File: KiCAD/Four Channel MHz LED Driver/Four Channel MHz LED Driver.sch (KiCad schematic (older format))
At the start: 39 parts

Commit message: First draft of Teensy pin allocation
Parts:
- added J?: Conn_01x05_Male, Custom Footprints:Ref_only, symbol Custom_parts:Conn_01x05_Male
- added J?: Conn_01x04_Male, Custom Footprints:Ref_only, symbol Custom_parts:Conn_01x04_Male
- added U?: Teensy3.6, symbol Custom_parts:Teensy3.6
- U?: value S18V20F12_12V_DC -> S34V32F12_12V_DC; footprint (none) -> Custom Footprints:S18V20F12_12V_DC
- U?: value ADP7118AUJZ-5.0-R7 -> ADP7134AUJZ-5.0-R7
- U? (x4): value TMUX1204DGSR -> TMUX1324DGSR
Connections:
- net 12V: now also J?.~ (Pin_4)
- net 3.3V: now also U?.15 (3.3V), U?.51 (3.3V)
- net 5V: now also U?.53 (VIN)
- net GND: now also RN?.2 (R2.1), RN?.4 (R4.1), RN?.6 (R6.1), RN?.8 (R8.1), J?.~ (Pin_4), J?.~ (Pin_5), U?.1 (GND), U?.39 (GND), U?.52 (AGND); no longer C?.1, RN?.11 (R6.2), RN?.13 (R4.2), RN?.15 (R2.2), RN?.9 (R8.2), U?.8 (GND), U?.9 (GND)
- net Isense_1: now also J?.1 (IN1), RN?.1 (R1.1); no longer RN?.16 (R1.2)
- net Isense_2: now also J?.2 (IN2), RN?.3 (R3.1); no longer RN?.14 (R3.2)
- net Isense_3: now also J?.1 (IN1), RN?.5 (R5.1); no longer RN?.12 (R5.2)
- net Isense_4: now also J?.2 (IN2), RN?.7 (R7.1); no longer RN?.10 (R7.2)
- net Vin: now also J?.~ (Pin_5)
- net SCK0: now reaches U?.10 (SCLK)
- net SCK0: now also U?.5 (SCK), U?.19 (27_RX1)
- net MOSI0: now reaches U?.8 (DIN)
- net MOSI0: now also U?.6 (SDI), U?.20 (28)
- net 25: now reaches U?.9 (~SYNC)
- net 25: now also U?.17 (25)
- net 24: now reaches U?.4 (*CS)
- net 24: now also U?.16 (24)
- net OA1_input: now reaches U?.8 (D)
- net OA2_input: now reaches U?.8 (D)
- net OA3_input: now reaches U?.8 (D)
- net OA4_input: now reaches U?.8 (D)
- net A-D_IO_1 renamed 35
- net 35: now also U?.32 (35_A16_PWM)
- net A-D_IO_2 renamed 34
- net 34: now also U?.31 (34_A15_RX5_CAN1TX_SDA0)
- net A-D_IO_3 renamed 33
- net 33: now also U?.30 (33_A14_TX5_CAN1TX_SCL0)
- net A-D_IO_4 renamed 32
- net 32: now also U?.24 (32_A13_TX4_SCK1)
- net analog_select_1 renamed 3
- net 3: now also U?.5 (3_PWM_CAN0TX_SCL2)
- net analog_select_2 renamed 5
- net 5: now also U?.7 (5_PWM_TX1_MISO1)
- net analog_select_3 renamed 7
- net 7: now also U?.9 (7_RX3_MISO0_SCL0)
- net analog_select_4 renamed 9
- net 9: now also U?.11 (9_PWM_RX2_CS0)
- net interline_1 renamed 2
- net 2: now also U?.4 (2_PWM)
- net interline_2 renamed 4
- net 4: now also U?.6 (4_PWM_CAN0RX_SDA2)
- net interline_3 renamed 6
- net 6: now also U?.8 (6_PWM)
- net interline_4 renamed 8
- net 8: now also U?.10 (8_TX3_MISO0_SDA0)
- new net: C?.1, U?.8 (GND), U?.9 (GND)
- new net A0_ADC0: RN?.13 (R4.2), RN?.14 (R3.2), U?.41 (14_A0_PWM_SCK0)
- new net A1_ADC0: RN?.15 (R2.2), RN?.16 (R1.2), U?.42 (15_A1_CS0_TOUCH)
- new net A33_DAC1: RN?.10 (R7.2), RN?.9 (R8.2), U?.37 (A21_DAC0)
- new net A34_DAC1: RN?.11 (R6.2), RN?.12 (R5.2), U?.38 (A22_DAC1)
- no-connect marks 3 -> 44
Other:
- note added: "----ADC0-----"
- note added: "----ADC1-----"
- note added: "A/D IO 1"
- note added: "A/D IO 2"
- note added: "A/D IO 3"
- note added: "A/D IO 4"
- note added: "Analog select 1\n"
- note added: "Analog select 2\n"
- note added: "Analog select 3\n"
- note added: "Analog select 4\n"
- note added: "Current sense voltage ouput"
- note added: "DAC CS"
- note added: "Digipot CS"
- note added: "Ext fan PWM"
- note added: "Ext temp"
- note added: "Header pins\nto connect\n12V SEPIC \nDC-DC \nconverter"
- note added: "Interline PWM 1"
- note added: "Interline PWM 2"
- note added: "Interline PWM 3"
- note added: "Interline PWM 4"
- note added: "Internal 4-channel ADC AWG with digipot current limit"
- note added: "Internal fan PWM"
- note added: "Isense_1"
- note added: "Isense_2"
- note added: "Isense_3"
- note added: "Isense_4"
- note added: "LED pot 1"
- note added: "LED pot 2"
- note added: "LED pot 3"
- note added: "LED pot 4"
- note added: "MOSFET temp 1"
- note added: "MOSFET temp 2"
- note added: "MOSFET temp 3"
- note added: "MOSFET temp 4"
- note added: "Manual/Auto Switch"
- note added: "Op-amp input mux"
- note added: "Pool external analog inputs"
- note added: "Resistor temp 1"
- note added: "Resistor temp 2"
- note added: "Resistor temp 3"
- note added: "Resistor temp 4"
- note added: "Status LED 1"
- note added: "Status LED 2"
- note added: "Status LED 3"
- note added: "Status LED 4"
- note added: "over-temp alarm"
- note removed: "Internal 4-channel AWG with current limit"
- moved on the sheet: C?, D?, J?, RN?, SW?, U?

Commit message: Reduce input impedance to 4.7k
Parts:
- removed RN?: 10k, Custom Footprints:Bourns_16-SOIC_8x_r-pack, symbol Device:R_Pack08
- added RN?: 4.7k, Custom Footprints:Bourns_16-SOIC_8x_r-pack, symbol Device:R_Pack08
- RN?: value 10k -> 4.7k; Part # 4816P-T01-103LF -> 4816P-T01-472LF
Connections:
- net GND: now also RN?.2 (R2.1), RN?.4 (R4.1), RN?.6 (R6.1), RN?.8 (R8.1)
- net Isense_1: now also RN?.1 (R1.1)
- net Isense_2: now also RN?.3 (R3.1)
- net Isense_3: now also RN?.5 (R5.1)
- net Isense_4: now also RN?.7 (R7.1)
- net A0_ADC0 renamed A0
- net A0: now also RN?.13 (R4.2), RN?.14 (R3.2)
- net A1_ADC0 renamed A1
- net A1: now also RN?.15 (R2.2), RN?.16 (R1.2)
- net A33_DAC1 renamed A33
- net A33: now also RN?.10 (R7.2), RN?.9 (R8.2)
- net A34_DAC1 renamed A34
- net A34: now also RN?.11 (R6.2), RN?.12 (R5.2)
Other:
- note added: "I/O maximum voltage: 27V"
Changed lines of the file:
@@
 P 2200 8150
 F 0 "RN?" V 1583 8150 50  0000 C CNN
-F 1 "10k" V 1674 8150 50  0000 C CNN
+F 1 "4.7k" V 1674 8150 50  0000 C CNN
 F 2 "Custom Footprints:Bourns_16-SOIC_8x_r-pack" V 2675 8150 50  0001 C CNN
 F 3 "file://media.digikey.com/api/videos/videoplayer/smallplayer/N0706.pdf" H 2200 8150 50  0001 C CNN
 F 4 "Bourns Inc." V 2200 8150 50  0001 C CNN "Manufacturer"
-F 5 "4816P-T01-103LF" V 2200 8150 50  0001 C CNN "Part #"
+F 5 "4816P-T01-472LF" V 2200 8150 50  0001 C CNN "Part #"
 	1    2200 8150
 	0    1    1    0
@@
 	1    1400 1600
 	0    -1   -1   0
-$EndComp
-$Comp
-L Device:R_Pack08 RN?
-U 1 1 5F51AB0E
-P 5350 9400
-F 0 "RN?" V 4733 9400 50  0000 C CNN
-F 1 "10k" V 4824 9400 50  0000 C CNN
-F 2 "Custom Footprints:Bourns_16-SOIC_8x_r-pack" V 5825 9400 50  0001 C CNN
-F 3 "file://media.digikey.com/api/videos/videoplayer/smallplayer/N0706.pdf" H 5350 9400 50  0001 C CNN
-F 4 "Bourns Inc." V 5350 9400 50  0001 C CNN "Manufacturer"
-F 5 "4816P-T01-103LF" V 5350 9400 50  0001 C CNN "Part #"
-	1    5350 9400
-	0    1    1    0
 $EndComp
 Text Label 5150 9000 2    50   ~ 0
@@
 Op-amp input mux
 Text Label 21950 2250 0    50   ~ 0
-A0_ADC0
+A0
 Text Label 21950 2550 0    50   ~ 0
-A34_DAC1
+A34
 Text Label 21950 2650 0    50   ~ 0
-A33_DAC1
+A33
 Text Label 19650 2850 2    50   ~ 0
 SCK0
@@
 MOSI0
 Text Label 5550 9050 0    50   ~ 0
-A1_ADC0
+A1
 Text Label 21950 2150 0    50   ~ 0
-A1_ADC0
+A1
 Text Label 5550 9250 0    50   ~ 0
-A0_ADC0
+A0
 Text Label 5550 9450 0    50   ~ 0
-A34_DAC1
+A34
 Text Label 5550 9650 0    50   ~ 0
-A33_DAC1
+A33
 Text Label 3950 5750 2    50   ~ 0
 SCK0
@@
 Text Notes 23100 3300 1    50   ~ 0
 ----ADC1-----
-Text Notes 18950 2350 0    50   ~ 0
+Text Notes 18650 2350 0    50   ~ 0
 Status LED 4
-Text Notes 18950 2250 0    50   ~ 0
+Text Notes 18650 2250 0    50   ~ 0
 Status LED 3
 Text Label 19650 2050 2    50   ~ 0
@@
 Text Label 19650 1750 2    50   ~ 0
 6
-Text Notes 18950 1250 0    50   ~ 0
+Text Notes 18600 1250 0    50   ~ 0
 Status LED 2
-Text Notes 18950 1150 0    50   ~ 0
+Text Notes 18600 1150 0    50   ~ 0
 Status LED 1
 Text Notes 19550 1950 2    50   ~ 0
@@
 Text Notes 18950 2050 0    50   ~ 0
 Analog select 4\n
+$Comp
+L Device:R_Pack08 RN?
+U 1 1 5F57894B
+P 5350 9400
+F 0 "RN?" V 4733 9400 50  0000 C CNN
+F 1 "4.7k" V 4824 9400 50  0000 C CNN
+F 2 "Custom Footprints:Bourns_16-SOIC_8x_r-pack" V 5825 9400 50  0001 C CNN
+F 3 "file://media.digikey.com/api/videos/videoplayer/smallplayer/N0706.pdf" H 5350 9400 50  0001 C CNN
+F 4 "Bourns Inc." V 5350 9400 50  0001 C CNN "Manufacturer"
+F 5 "4816P-T01-472LF" V 5350 9400 50  0001 C CNN "Part #"
+	1    5350 9400
+	0    1    1    0
+$EndComp
+Text Notes 900  8700 1    59   ~ 0
+I/O maximum voltage: 27V
 $EndSCHEMATC

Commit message: Update license
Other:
- note added: "Distribute external analog inputs"
- note removed: "Pool external analog inputs"
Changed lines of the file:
@@
 Text Notes 2900 8450 2    50   ~ 0
 A/D IO 4
-Text Notes 3800 7650 0    59   ~ 0
-Pool external analog inputs
+Text Notes 3600 7650 0    59   ~ 0
+Distribute external analog inputs
 Text Notes 22250 1450 0    50   ~ 0
 LED pot 2

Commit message: Split analog inputs between ADC0 and ADC1
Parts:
- U?: value MCP4351-502E_ST -> MCP4211-502E_ST
- U?: value S34V32F12_12V_DC -> S20V18F12_12V_DC
- U?: value ADP7134AUJZ-5.0-R7 -> ADP7120AUJZ-5.0-R7
- U? (x4): value TMUX1324DGSR -> TMUX1184DGSR
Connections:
- removed net 32: D?.3, RN?.9 (R8.2), U?.24 (32_A13_TX4_SCK1)
- removed net 33: D?.6, RN?.10 (R7.2), U?.30 (33_A14_TX5_CAN1TX_SCL0)
- removed net 34: D?.3, RN?.11 (R6.2), U?.31 (34_A15_RX5_CAN1TX_SDA0)
- removed net 35: D?.6, RN?.12 (R5.2), U?.32 (35_A16_PWM)
- net A0: no longer names the net of RN?.13 (R4.2), RN?.14 (R3.2)
- net A0: no longer U?.41 (14_A0_PWM_SCK0)
- net A1: no longer names the net of RN?.15 (R2.2), RN?.16 (R1.2)
- net A1: no longer U?.42 (15_A1_CS0_TOUCH)
- net A33: no longer names the net of RN?.10 (R7.2), RN?.9 (R8.2)
- net A33: no longer U?.37 (A21_DAC0)
- net A34: no longer names the net of RN?.11 (R6.2), RN?.12 (R5.2)
- net A34: no longer U?.38 (A22_DAC1)
- new net 18: RN?.9 (R8.2)
- new net 19: RN?.10 (R7.2)
- new net 20: RN?.11 (R6.2)
- new net 21: RN?.12 (R5.2)
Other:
- note added: "-------ADC0------"
- note added: "--ADC1--"
- note added: "ADC0"
- note added: "ADC1"
- note added: "I/O maximum voltage: 27V (160mW)\nNiDaq PCI-6110 is +/- 10V 5mA\nTherefore, minimum impedance is 2000 Ohms"
- note added: "https://forum.pjrc.com/attachment.php?attachmentid=10666&d=1495536536"
- note removed: "----ADC0-----"
- note removed: "----ADC1-----"
- note removed: "I/O maximum voltage: 27V"
- moved on the sheet: D?, U?

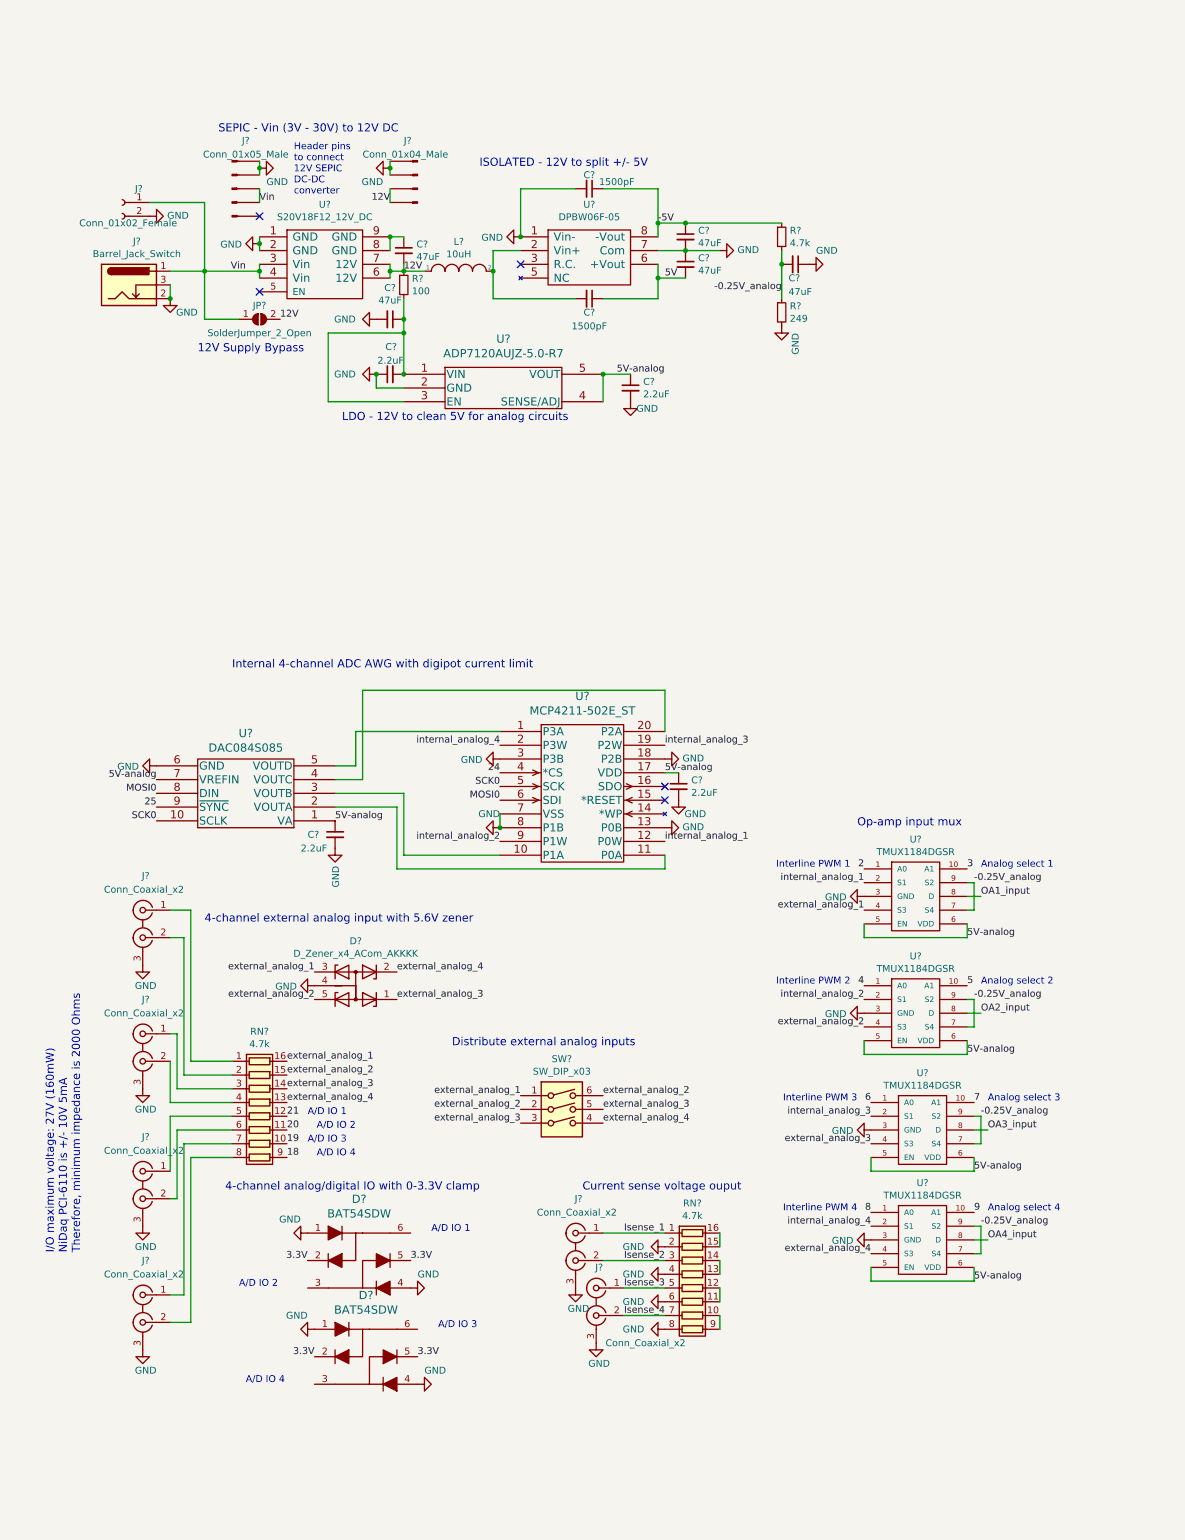
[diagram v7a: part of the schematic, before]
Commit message: Add LED connectors switch to RJ45 for IO
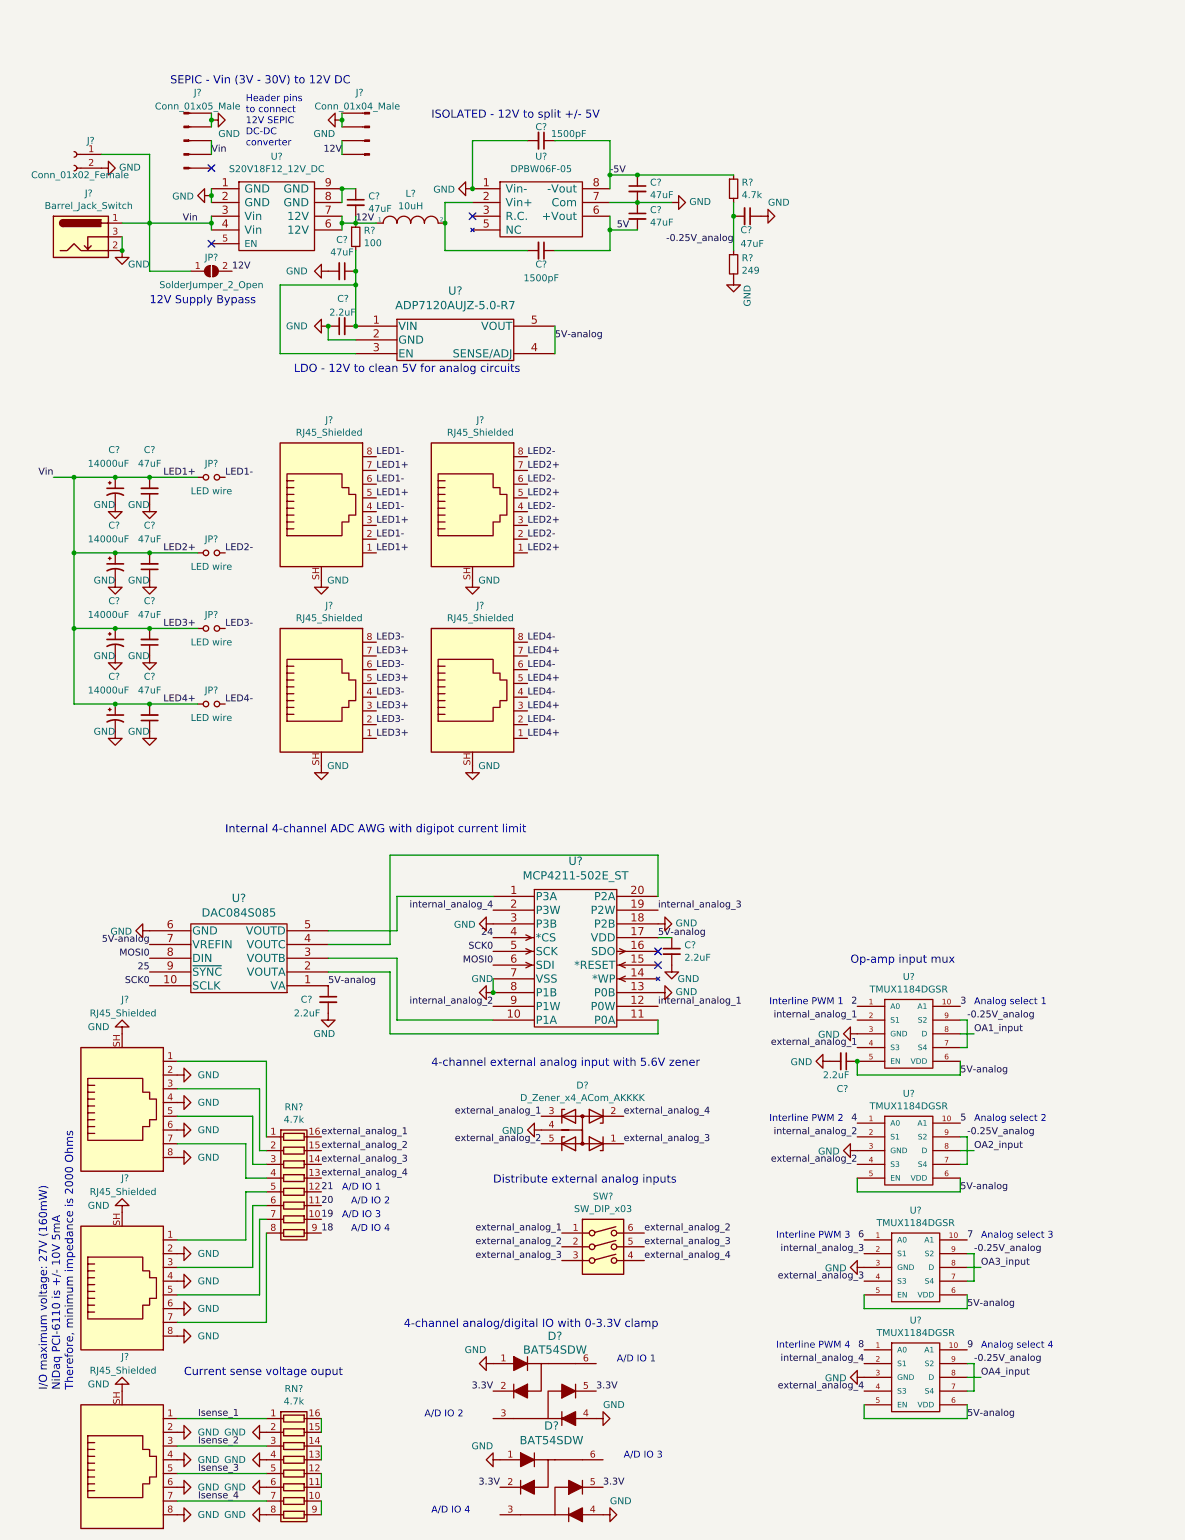
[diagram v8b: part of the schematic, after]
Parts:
- removed C?: 2.2uF, Custom Footprints:0508_Capacitor, symbol Device:C_Small
- removed J? (x6): Conn_Coaxial_x2, Custom Footprints:031-6575_2x_BNC, symbol Connector:Conn_Coaxial_x2
- added C? (x4): 14000uF, Capacitor_THT:CP_Radial_D18.0mm_P7.50mm, symbol Device:CP1_Small
- added C? (x4): 47uF, Capacitor_SMD:C_1206_3216Metric, symbol Device:C_Small
- added C?: 2.2uF, Custom Footprints:0508_Capacitor, symbol Device:C_Small
- added J? (x7): RJ45_Shielded, Custom Footprints:Molex_RJ45_855437001, symbol Connector:RJ45_Shielded
- added JP? (x4): LED wire, Connector_Wire:SolderWire-2.5sqmm_1x02_P7.2mm_D2.4mm_OD3.6mm, symbol Device:Jumper_NO_Small
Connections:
- net Vin is gone; now on net LED1+: J?.1, J?.1 (Pin_1), J?.~ (Pin_5), JP?.1 (A), U?.3 (Vin), U?.4 (Vin)
- net 5V-analog: now also C?.1
- net GND: now also C?.1, C?.1, C?.1, C?.1, C?.2, C?.2, C?.2, C?.2, C?.2, J?.2, J?.2, J?.2, J?.4, J?.4, J?.4, J?.6, J?.6, J?.6, J?.8, J?.8, J?.8, J?.SH, J?.SH, J?.SH, J?.SH, J?.SH, J?.SH, J?.SH
- net Isense_1: now also J?.1
- net Isense_2: now also J?.3
- net Isense_3: now also J?.5
- net Isense_4: now also J?.7
- net at RN?.3 (R3.1): now also J?.5
- net at RN?.4 (R4.1): now also J?.7
- net at RN?.1 (R1.1): now also J?.1
- net at RN?.2 (R2.1): now also J?.3
- net at RN?.7 (R7.1): now also J?.5
- net at RN?.8 (R8.1): now also J?.7
- net at RN?.5 (R5.1): now also J?.1
- net at RN?.6 (R6.1): now also J?.3
- net LED1+: now reaches J?.~ (Pin_5)
- net LED1+: now also C?.1, C?.1, C?.1, C?.1, C?.2, C?.2, C?.2, C?.2, J?.1, J?.1, J?.1, J?.1, J?.3, J?.3, J?.3, J?.3, J?.5, J?.5, J?.5, J?.5, J?.7, J?.7, J?.7, J?.7, JP?.1, JP?.1, JP?.1, JP?.1
- new net LED1-: J?.2, J?.4, J?.6, J?.8, JP?.2
- new net LED2-: J?.2, J?.4, J?.6, J?.8, JP?.2
- new net LED3-: J?.2, J?.4, J?.6, J?.8, JP?.2
- new net LED4-: J?.2, J?.4, J?.6, J?.8, JP?.2
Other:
- moved on the sheet: C?, D?, J?, JP?, L?, R?, RN?, SW?, U?
